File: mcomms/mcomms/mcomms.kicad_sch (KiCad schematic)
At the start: 47 parts, among them J1 Conn_01x03_Pin, J2 Conn_01x04_Pin, J3 Conn_01x02_Pin, J4 Conn_01x02_Pin, J5 Conn_01x03_Pin, Q1 SI2300DS, Q2 SI2300DS, Q3 SI2300DS, Q4 SI2300DS

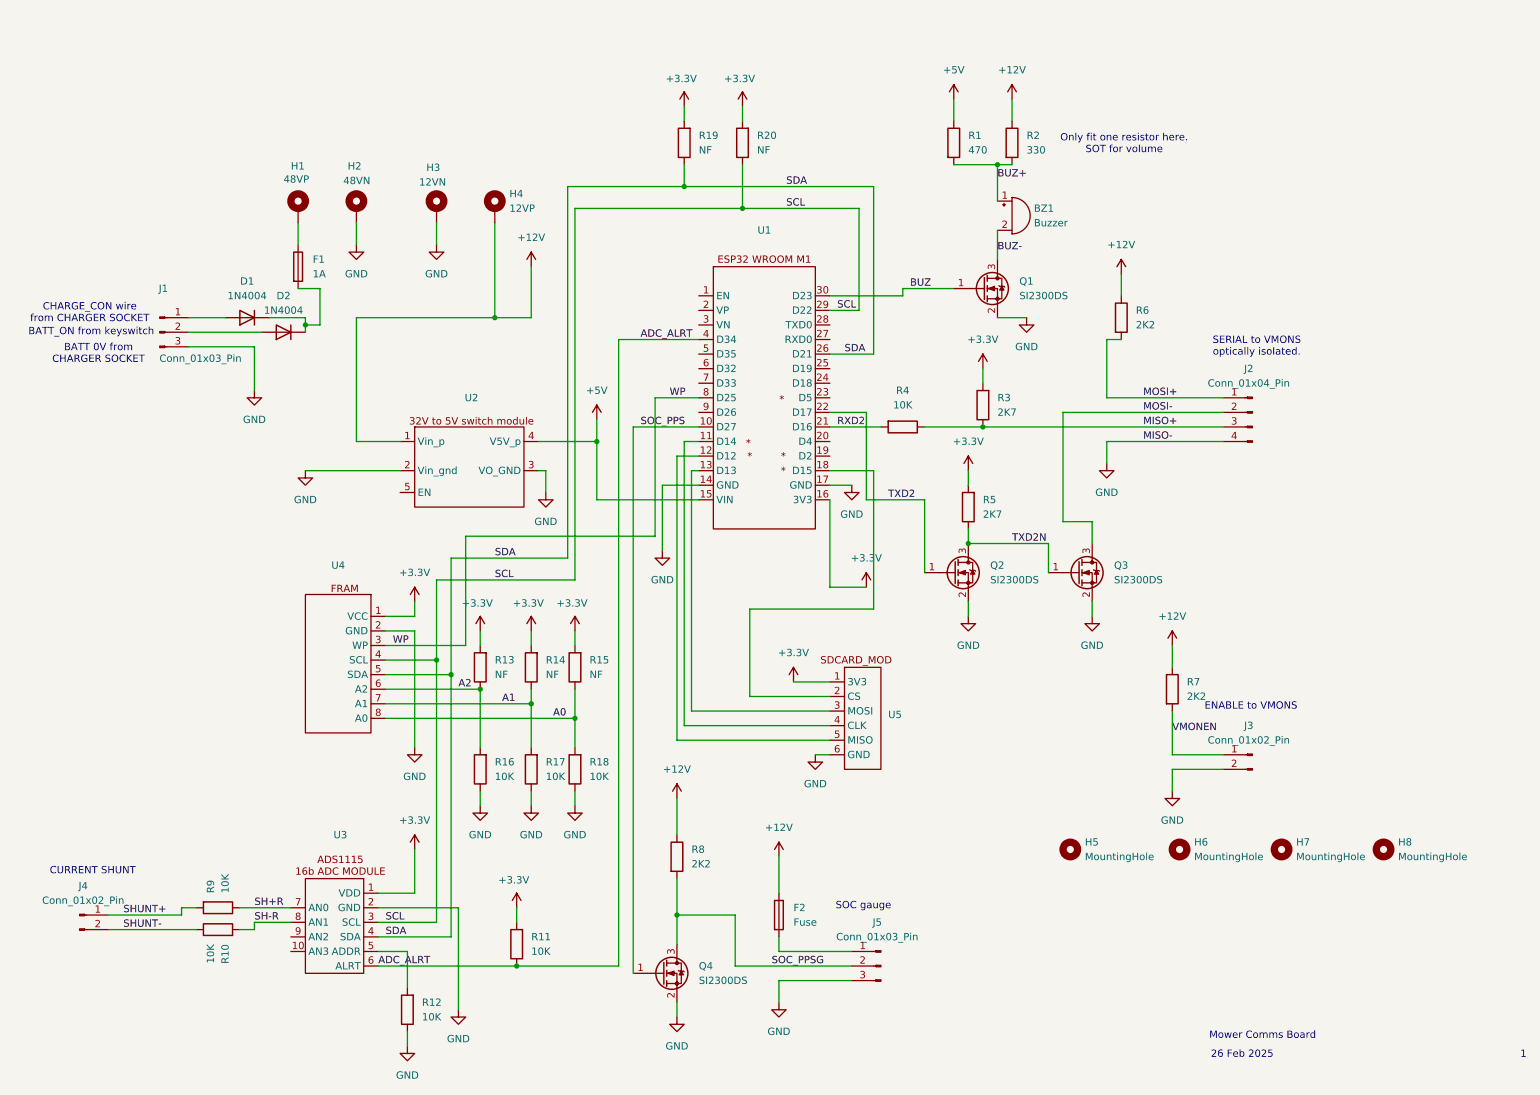
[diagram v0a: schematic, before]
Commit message: add a top level schematic
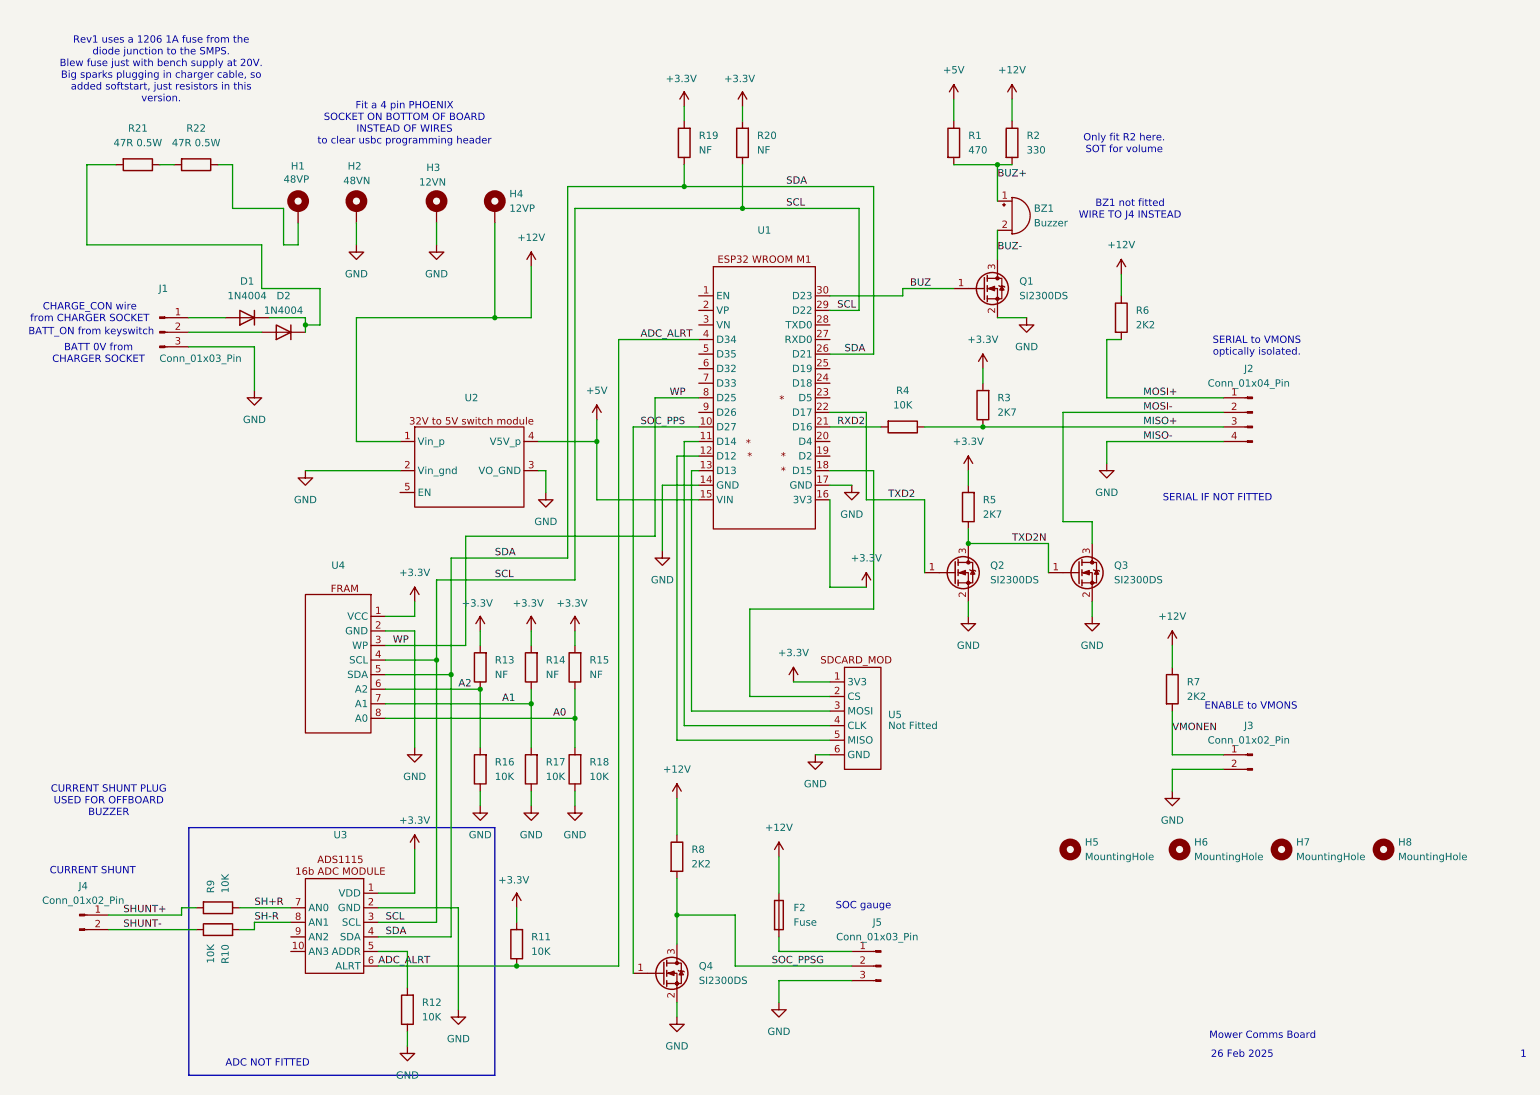
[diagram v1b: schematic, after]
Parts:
- removed F1: 1A, Fuse:Fuse_1206_3216Metric_Pad1.42x1.75mm_HandSolder, symbol Device:Fuse
- added R21, R22: 47R 0.5W, Resistor_SMD:R_0805_2012Metric_Pad1.20x1.40mm_HandSolder, symbol Device:R
- U5: value ~ -> Not Fitted
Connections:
- net at H1.1: now also R22.1
- net at D1.1 (K), D2.1 (K): now also R21.2
- new net: R21.1, R22.2
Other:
- note added: "ADC NOT FITTED"
- note added: "BZ1 not fitted WIRE TO J4 INSTEAD"
- note added: "CURRENT SHUNT PLUG USED FOR OFFBOARD BUZZER"
- note added: "Fit a 4 pin PHOENIX SOCKET ON BOTTOM OF BOARD INSTEAD OF WIRES to clear usbc programming header"
- note added: "Only fit R2 here. SOT for volume"
- note added: "Rev1 uses a 1206 1A fuse from the diode junction to the SMPS. Blew fuse just with bench supply at 20V. Big sparks plugging in charger cable, so added softstart, just resistors in this version."
- note added: "SERIAL IF NOT FITTED"
- note removed: "Only fit one resistor here. SOT for volume"

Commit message: realized the charger_connected mod to mco wasn't on the schematic
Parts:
- added R23: 1M, Resistor_SMD:R_0805_2012Metric_Pad1.20x1.40mm_HandSolder, symbol Device:R
- added R24: 68K, Resistor_SMD:R_0805_2012Metric_Pad1.20x1.40mm_HandSolder, symbol Device:R
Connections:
- net GND: now also R24.1
- net CHARGER_CONNECTED: now reaches U1.5 (D35)
- net CHARGER_CONNECTED: now also R23.2, R24.2
- net at D1.2 (A), J1.1 (Pin_1): now also R23.1
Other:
- note added: "Charger_connected was added after Rev1 PCB was drawn"
